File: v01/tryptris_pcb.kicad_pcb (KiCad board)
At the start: 2 copper layers, 298.8 x 122 mm, 131 parts, among them J1 USB_C_Receptacle_USB2.0, J2 I2C-L, J3 I2C-R, SW1 Reset, U1 ATmega32U4-AU, U2 MCP23017_SO, Y1 16Mhz

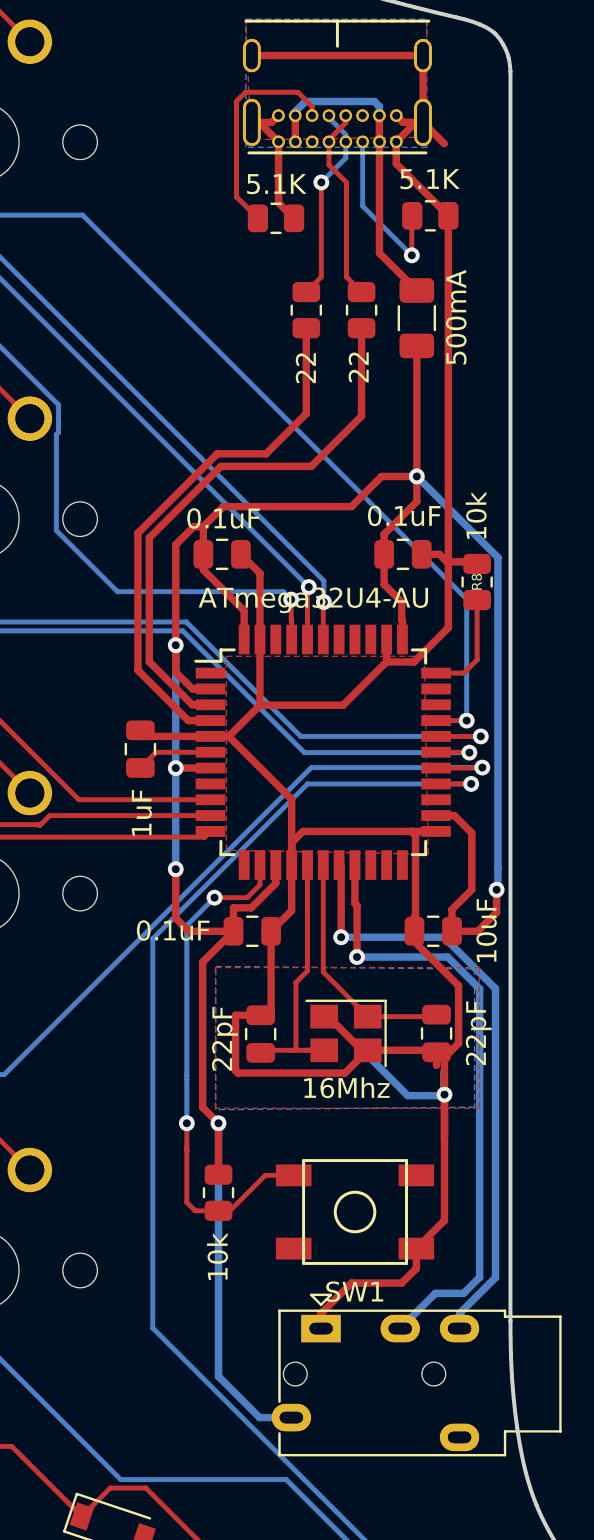
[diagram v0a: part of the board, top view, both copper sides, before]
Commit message: Improve USB data lines
Reroute to get more equal lengths.
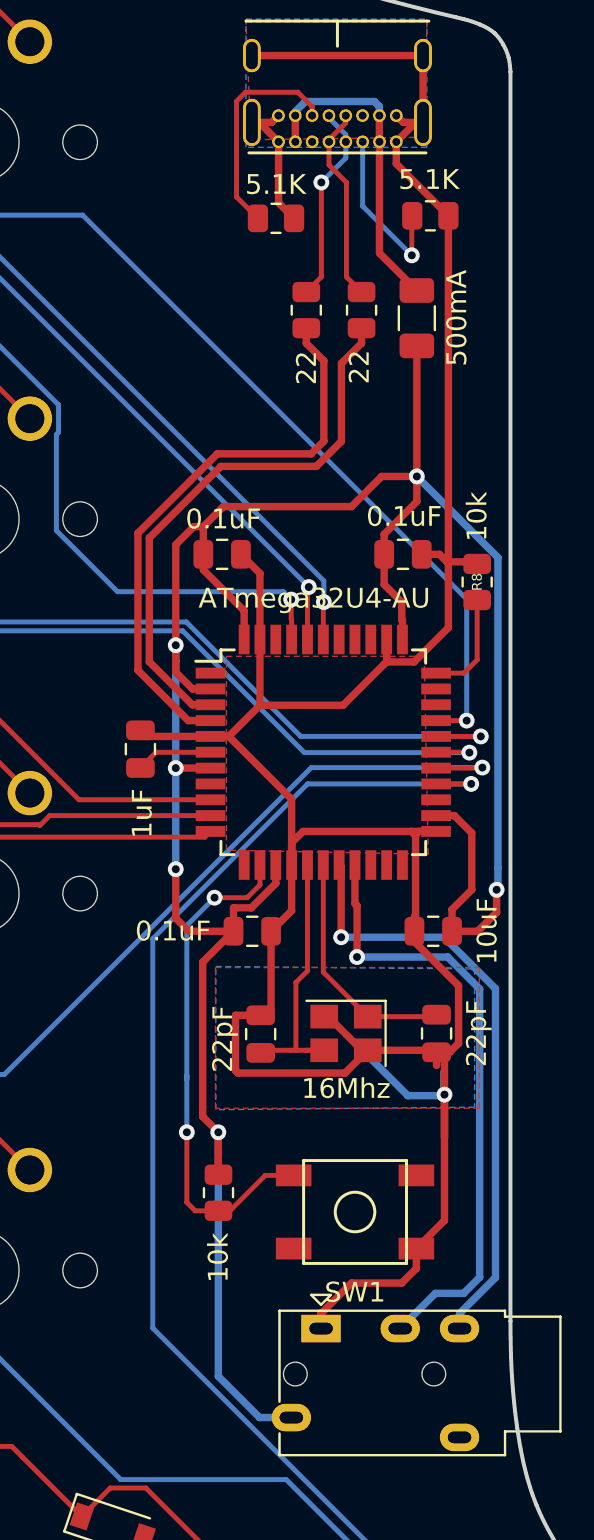
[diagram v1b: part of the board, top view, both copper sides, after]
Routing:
- net D+: track 27.0 -> 29.1 mm
- net GND: track 163.2 -> 161.7 mm
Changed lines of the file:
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@@
     (thickness 1.6)
     (drawings 358)
-    (tracks 855)
+    (tracks 858)
     (zones 0)
     (modules 131)
@@
   (segment (start 152.2508 46.1708) (end 154.884 48.804) (width 0.375) (layer F.Cu) (net 1))
   (segment (start 152.2508 45.0636) (end 152.2508 46.1708) (width 0.375) (layer F.Cu) (net 1))
-  (segment (start 153.6008 44.0836) (end 154.676829 45.159629) (width 0.375) (layer F.Cu) (net 1))
   (segment (start 207.342 83.82) (end 206.121 83.82) (width 0.375) (layer F.Cu) (net 120))
   (segment (start 206.121 83.82) (end 205.74 83.439) (width 0.375) (layer F.Cu) (net 120))
@@
   (segment (start 144.023 84.963) (end 142.465 86.521) (width 0.375) (layer F.Cu) (net 5))
   (segment (start 142.465 86.521) (end 142.465 93.865) (width 0.375) (layer F.Cu) (net 5))
-  (segment (start 143.265 94.665) (end 143.265 97.265) (width 0.375) (layer F.Cu) (net 5))
-  (segment (start 142.465 93.865) (end 143.265 94.665) (width 0.375) (layer F.Cu) (net 5))
-  (via (at 143.265 94.665) (size 0.8) (drill 0.4) (layers F.Cu B.Cu) (net 5))
-  (segment (start 143.265 94.665) (end 143.265 107.465) (width 0.375) (layer B.Cu) (net 5))
-  (segment (start 145.3408 109.5408) (end 146.948 109.5408) (width 0.375) (layer B.Cu) (net 5))
-  (segment (start 143.265 107.465) (end 145.3408 109.5408) (width 0.375) (layer B.Cu) (net 5))
   (segment (start 146.162 82.540798) (end 146.162 81.616) (width 0.375) (layer F.Cu) (net 5))
   (segment (start 144.925289 83.777509) (end 146.162 82.540798) (width 0.375) (layer F.Cu) (net 5))
@@
   (segment (start 141.105 65.425) (end 141.105 70.505) (width 0.375) (layer F.Cu) (net 5))
   (segment (start 142.019 64.511) (end 141.105 65.425) (width 0.375) (layer F.Cu) (net 5))
+  (segment (start 142.465 93.865) (end 142.465 94.332) (width 0.375) (layer F.Cu) (net 5))
+  (via (at 143.256 95.123) (size 0.8) (drill 0.4) (layers F.Cu B.Cu) (net 5))
+  (segment (start 142.465 94.332) (end 143.256 95.123) (width 0.375) (layer F.Cu) (net 5))
+  (segment (start 145.3408 109.5408) (end 146.948 109.5408) (width 0.375) (layer B.Cu) (net 5))
+  (segment (start 143.256 107.456) (end 145.3408 109.5408) (width 0.375) (layer B.Cu) (net 5))
+  (segment (start 143.256 95.123) (end 143.256 107.456) (width 0.375) (layer B.Cu) (net 5))
+  (segment (start 143.256 97.256) (end 143.265 97.265) (width 0.375) (layer F.Cu) (net 5))
+  (segment (start 143.256 95.123) (end 143.256 97.256) (width 0.375) (layer F.Cu) (net 5))
   (segment (start 35.56 41.656) (end 38.735 44.831) (width 0.25) (layer F.Cu) (net 6))
   (segment (start 33.145 41.656) (end 35.56 41.656) (width 0.25) (layer F.Cu) (net 6))
@@
   (segment (start 145.629 97.301) (end 147.066 97.301) (width 0.25) (layer F.Cu) (net 91))
   (segment (start 143.84 99.09) (end 145.629 97.301) (width 0.25) (layer F.Cu) (net 91))
-  (segment (start 141.665 92.465) (end 141.665 94.665) (width 0.25) (layer B.Cu) (net 91))
-  (via (at 141.665 94.665) (size 0.8) (drill 0.4) (layers F.Cu B.Cu) (net 91))
-  (segment (start 141.665 94.665) (end 141.665 96.065) (width 0.25) (layer F.Cu) (net 91))
-  (segment (start 141.665 96.065) (end 141.665 98.665) (width 0.25) (layer F.Cu) (net 91))
-  (segment (start 141.665 95.865) (end 141.665 96.065) (width 0.25) (layer F.Cu) (net 91))
-  (segment (start 141.939498 73.516) (end 142.862 73.516) (width 0.375) (layer F.Cu) (net 92))
-  (segment (start 139.76701 71.343512) (end 141.939498 73.516) (width 0.375) (layer F.Cu) (net 92))
-  (segment (start 139.76701 65.08399) (end 139.76701 71.343512) (width 0.375) (layer F.Cu) (net 92))
+  (via (at 141.665 95.123) (size 0.8) (drill 0.4) (layers F.Cu B.Cu) (net 91))
+  (segment (start 141.665 95.123) (end 141.665 98.665) (width 0.25) (layer F.Cu) (net 91))
+  (segment (start 141.665 92.265) (end 141.665 95.123) (width 0.25) (layer B.Cu) (net 91))
   (segment (start 150.368 54.483) (end 150.495 54.483) (width 0.375) (layer F.Cu) (net 92))
+  (segment (start 149.479 56.261) (end 150.495 55.245) (width 0.375) (layer F.Cu) (net 92))
+  (segment (start 149.479 60.198) (end 149.479 56.261) (width 0.375) (layer F.Cu) (net 92))
+  (segment (start 143.383 61.468) (end 148.209 61.468) (width 0.375) (layer F.Cu) (net 92))
+  (segment (start 150.495 55.245) (end 150.495 54.483) (width 0.375) (layer F.Cu) (net 92))
   (segment (start 139.76701 65.08399) (end 143.383 61.468) (width 0.375) (layer F.Cu) (net 92))
-  (segment (start 143.383 61.468) (end 147.955 61.468) (width 0.375) (layer F.Cu) (net 92))
-  (segment (start 150.495 58.928) (end 150.495 54.483) (width 0.375) (layer F.Cu) (net 92))
-  (segment (start 147.955 61.468) (end 150.495 58.928) (width 0.375) (layer F.Cu) (net 92))
+  (segment (start 139.76701 71.343512) (end 139.76701 65.08399) (width 0.375) (layer F.Cu) (net 92))
+  (segment (start 141.939498 73.516) (end 139.76701 71.343512) (width 0.375) (layer F.Cu) (net 92))
+  (segment (start 148.209 61.468) (end 149.479 60.198) (width 0.375) (layer F.Cu) (net 92))
+  (segment (start 142.862 73.516) (end 141.939498 73.516) (width 0.375) (layer F.Cu) (net 92))
+  (segment (start 141.737 74.316) (end 142.862 74.316) (width 0.375) (layer F.Cu) (net 93))
   (segment (start 139.192 71.771) (end 141.737 74.316) (width 0.375) (layer F.Cu) (net 93))
   (segment (start 139.192 64.845814) (end 139.192 71.771) (width 0.375) (layer F.Cu) (net 93))
   (segment (start 143.204814 60.833) (end 139.192 64.845814) (width 0.375) (layer F.Cu) (net 93))
-  (segment (start 145.669 60.833) (end 143.204814 60.833) (width 0.375) (layer F.Cu) (net 93))
-  (segment (start 141.737 74.316) (end 142.862 74.316) (width 0.375) (layer F.Cu) (net 93))
-  (segment (start 147.701 58.801) (end 145.669 60.833) (width 0.375) (layer F.Cu) (net 93))
-  (segment (start 147.701 54.483) (end 147.701 58.801) (width 0.375) (layer F.Cu) (net 93))
+  (segment (start 147.955 60.833) (end 143.204814 60.833) (width 0.375) (layer F.Cu) (net 93))
+  (segment (start 148.59 60.198) (end 147.955 60.833) (width 0.375) (layer F.Cu) (net 93))
+  (segment (start 148.59 56.134) (end 148.59 60.198) (width 0.375) (layer F.Cu) (net 93))
+  (segment (start 147.701 55.245) (end 148.59 56.134) (width 0.375) (layer F.Cu) (net 93))
+  (segment (start 147.701 54.483) (end 147.701 55.245) (width 0.375) (layer F.Cu) (net 93))
   (segment (start 154.262 71.916) (end 155.668 71.916) (width 0.25) (layer F.Cu) (net 94))
   (segment (start 156.337 71.247) (end 156.337 68.2225) (width 0.25) (layer F.Cu) (net 94))

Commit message: Add center 'card' and mousebites.
These help keep the board together. I'm thinking the card could
either make several keychain items, or a small piece of art.
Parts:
- added mouse-bite-2mm-slot: VAL**, Panelization:mouse-bite-2mm-slot, F.Cu at (193.0, 102.6)
- added mouse-bite-2mm-slot: VAL**, Panelization:mouse-bite-2mm-slot, F.Cu at (192.9, 44.3)
- added mouse-bite-2mm-slot: VAL**, Panelization:mouse-bite-2mm-slot, F.Cu at (159.0, 102.6)
- added mouse-bite-2mm-slot: VAL**, Panelization:mouse-bite-2mm-slot, F.Cu at (159.0, 44.3)
- moved R9 0.27 mm to (199.0, 99.8)
- moved R10 0.25 mm to (202.1, 99.8)
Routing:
- net (no net): track 12.0 -> 0.00 mm
- net Row4-R: track 115.2 -> 108.3 mm
- net Row0-R: track 146.7 -> 151.6 mm
- net VBUS: track 86.1 -> 88.2 mm, vias 2 -> 3
- net Col6: track 114.8 -> 116.8 mm
- net Col7: track 128.7 -> 130.0 mm
- net SDA-L: track 31.2 -> 30.4 mm
- net Col10: track 151.8 -> 152.5 mm
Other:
- outline, holes or cut-outs redrawn

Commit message: Add label.
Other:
- board text added: "Tryptris rev01 : markstory"
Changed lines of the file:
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@@
   (general
     (thickness 1.6)
-    (drawings 380)
+    (drawings 381)
     (tracks 885)
     (zones 0)
@@
     )
   )
+  (gr_text "Tryptris rev01 : markstory" (at 39.0017 113.4618) (layer B.SilkS)
+    (effects (font (size 1 1) (thickness 0.15)) (justify mirror))
+  )
   (gr_line (start 162.56 109.6137) (end 189.4078 109.5954) (layer Edge.Cuts) (width 0.2))

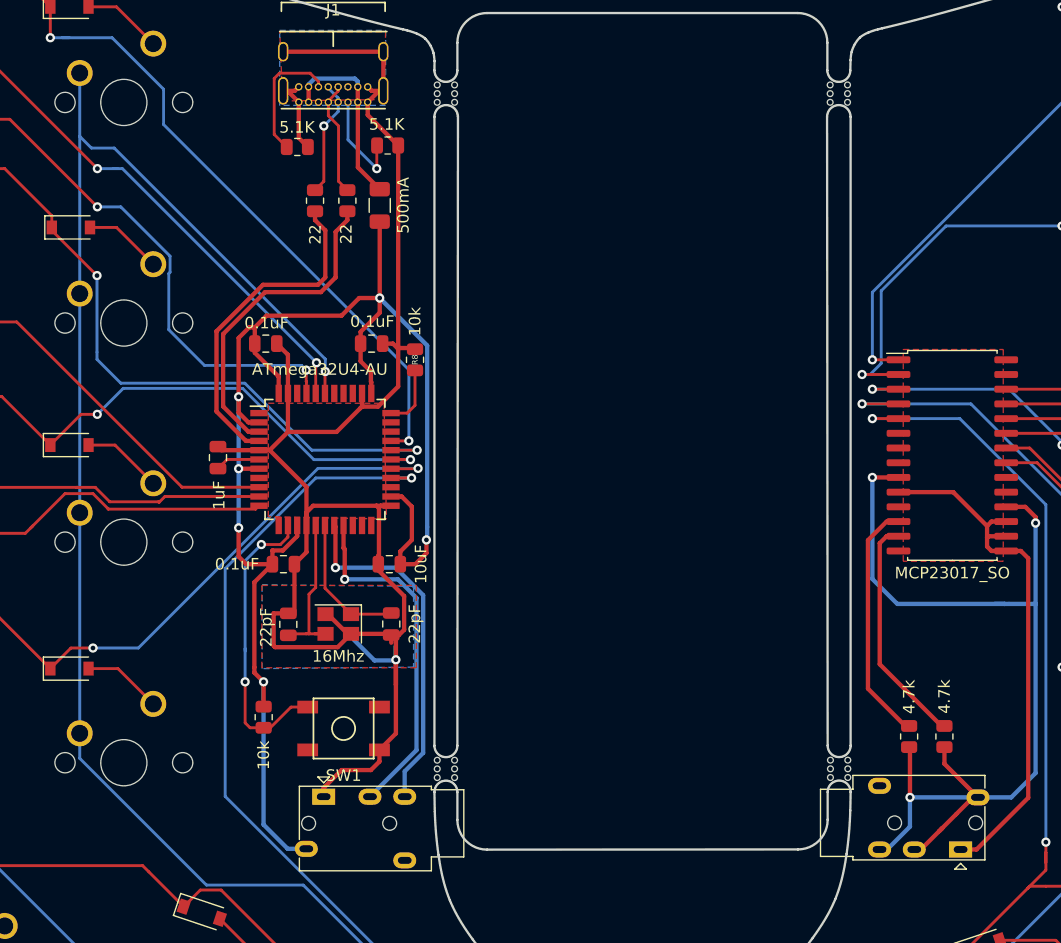
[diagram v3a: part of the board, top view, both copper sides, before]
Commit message: Fix TRRS wiring and improve grounding
* Don't route gnd for trrs through the crystal. Instead send it around the
  crystal and into the larger ground plane of the MCU.
* Fix the right side wiring. 5V should pass through the resisitors
  before being connected to the signal wires. The goal is to provide
  background voltage not flood the signal.
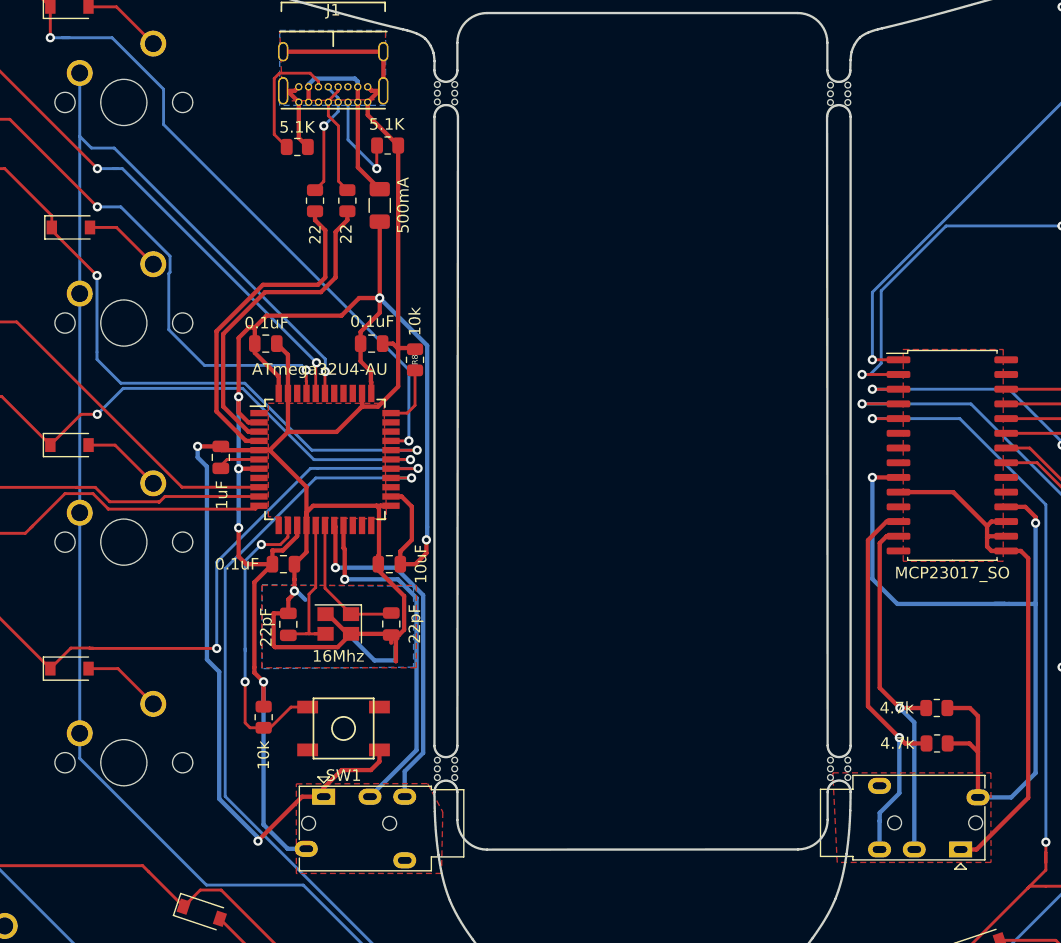
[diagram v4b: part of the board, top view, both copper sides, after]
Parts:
- removed the mouse-bite-2mm-slot at (193.0, 102.6)
- removed the mouse-bite-2mm-slot at (192.9, 44.3)
- removed the mouse-bite-2mm-slot at (159.0, 102.6)
- removed the mouse-bite-2mm-slot at (159.0, 44.3)
- added mouse-bite-2mm-slot: VAL**, Panelization:mouse-bite-2mm-slot, F.Cu at (193.0, 102.6)
- added mouse-bite-2mm-slot: VAL**, Panelization:mouse-bite-2mm-slot, F.Cu at (193.0, 44.3)
- added mouse-bite-2mm-slot: VAL**, Panelization:mouse-bite-2mm-slot, F.Cu at (159.0, 44.3)
- added mouse-bite-2mm-slot: VAL**, Panelization:mouse-bite-2mm-slot, F.Cu at (159.0, 102.6)
- moved R10 2.55 mm to (201.4, 97.4), turned to 0 degrees
- moved R9 2.49 mm to (201.4, 100.4), turned to 0 degrees
- moved C3 0.25 mm to (139.6, 75.7)
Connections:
- J3 pad R1: VBUS -> SDA-R
- J3 pad R2: VBUS -> SCL-R
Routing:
- net GND: track 161.7 -> 198.5 mm, vias 1 -> 3
- net VBUS: track 88.2 -> 71.5 mm, vias 3 -> 2
- net SCL-R: track 20.8 -> 35.5 mm, vias 0 -> 1
- net SDA-R: track 19.9 -> 32.9 mm, vias 0 -> 1
- net Row3-L: track 150.2 -> 154.9 mm
